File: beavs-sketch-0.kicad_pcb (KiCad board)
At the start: 2 copper layers, 25 parts, among them J1 USB_C_Receptacle_USB2.0_16P, J10 Conn_01x03, J11 Conn_01x03, J2 Conn_Coaxial, J3 Micro_SD_Card_Det2, J4 Conn_Coaxial, J5 Conn_01x02, J6 Conn_01x03, J7 Conn_01x03, J8 Conn_01x03, J9 Conn_01x03, U1 RP2040, U2 W25Q128JVS, U3 MS5607-02BA, U4 RFM95W-915S2, U5 MAX-M10S, Y1 Crystal_GND24

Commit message: do some schematic work
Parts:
- removed REF**: JST_VH_B3P-VH-B_1x03_P3.96mm_Vertical, Connector_JST:JST_VH_B3P-VH-B_1x03_P3.96mm_Vertical
- added C10: 100n, Capacitor_SMD:C_0402_1005Metric, F.Cu at (204.8, 132.0)
- added C11: 1u, Capacitor_SMD:C_0402_1005Metric, F.Cu at (211.0, 130.1)
- added C12: 100n, Capacitor_SMD:C_0402_1005Metric, F.Cu at (200.7, 128.0)
- added C13: 100n, Capacitor_SMD:C_0402_1005Metric, F.Cu at (210.9, 126.3)
- added C14: 100n, Capacitor_SMD:C_0402_1005Metric, F.Cu at (200.3, 126.8)
- added C4: 100n, Capacitor_SMD:C_0402_1005Metric, F.Cu at (210.2, 154.4)
- added C5: 100n, Capacitor_SMD:C_0402_1005Metric, F.Cu at (207.9, 154.9)
- added C6: 1u, Capacitor_SMD:C_0402_1005Metric, F.Cu at (210.0, 130.1)
- added C7: 100n, Capacitor_SMD:C_0402_1005Metric, F.Cu at (209.1, 131.1)
- added C8: 100n, Capacitor_SMD:C_0402_1005Metric, F.Cu at (204.7, 120.3)
- added C9: 100n, Capacitor_SMD:C_0402_1005Metric, F.Cu at (208.7, 120.7)
- added J12: Micro_SD_Card, Connector_Card:microSD_HC_Molex_47219-2001, F.Cu at (205.1, 141.7)
- added NT1: NetTie_2, NetTie:NetTie-2_SMD_Pad2.0mm, F.Cu at (183.8, 56.6)
- added Q2: SiS427EDN, Package_SO:Vishay_PowerPAK_1212-8_Single, F.Cu at (188.0, 46.5)
- added R2: R_Small, Resistor_SMD:R_0402_1005Metric, F.Cu at (191.2, 45.3)
- added R3: 5.1k, Resistor_SMD:R_0402_1005Metric, F.Cu at (214.0, 142.0)
- added R4: DNF, Resistor_SMD:R_0402_1005Metric, F.Cu at (207.5, 131.4)
- added R5: 5.1k, Resistor_SMD:R_0402_1005Metric, F.Cu at (214.0, 130.2)
- added U10: INA745A, beavs-footprints:QFN-14-REL_TI, F.Cu at (193.4, 82.6)
- added U11: INA745A, beavs-footprints:QFN-14-REL_TI, F.Cu at (193.4, 93.2)
- added U12: INA745A, beavs-footprints:QFN-14-REL_TI, F.Cu at (193.4, 103.7)
- added U13: INA745A, beavs-footprints:QFN-14-REL_TI, F.Cu at (193.4, 114.2)
- added U14: ISM6HG256X, Package_LGA:LGA-14_3x2.5mm_P0.5mm_LayoutBorder3x4y, F.Cu at (207.9, 152.9)
- added U15: SN74LVC8T245, Package_SO:TSSOP-24_4.4x7.8mm_P0.65mm, F.Cu at (191.4, 133.3)
- added U6: INA745A, beavs-footprints:QFN-14-REL_TI, F.Cu at (193.4, 61.1)
- added U7: AMS1117-3.3, Package_TO_SOT_SMD:SOT-223-3_TabPin2, F.Cu at (221.7, 113.0)
- added U8: AMS1117-5.0, Package_TO_SOT_SMD:SOT-223-3_TabPin2, F.Cu at (214.0, 113.0)
- added U9: INA745A, beavs-footprints:QFN-14-REL_TI, F.Cu at (193.4, 71.6)
- J10, J11, J6, J7, J8, J9: footprint Connector_JST:JST_XH_B3B-XH-AM_1x03_P2.50mm_Vertical -> Connector_JST:JST_VH_B3P-VH-B_1x03_P3.96mm_Vertical
- J3: value Micro_SD_Card_Det2 -> Conn_01x02; footprint Connector_Card:microSD_HC_Hirose_DM3AT-SF-PEJM5 -> Connector_AMASS:AMASS_XT30UPB-F_1x02_P5.0mm_Vertical
- J5: footprint Connector_JST:JST_XH_S2B-XH-A-1_1x02_P2.50mm_Horizontal -> Connector_JST:JST_XH_B2B-XH-A_1x02_P2.50mm_Vertical
- moved D1 90.5 mm to (180.2, 160.8), turned to -90 degrees
- moved D2 87.8 mm to (180.2, 157.3), turned to -90 degrees
- moved D3 85.3 mm to (180.2, 153.7), turned to -90 degrees
- moved D4 83.0 mm to (180.2, 150.2), turned to -90 degrees
- moved D5 81.0 mm to (180.2, 146.6), turned to -90 degrees
- moved D6 79.3 mm to (180.2, 143.1), turned to -90 degrees
- moved J5 68.3 mm to (182.3, 129.2), turned to 90 degrees
- moved R1 66.7 mm to (200.6, 125.8)
- moved J1 53.9 mm to (218.4, 136.0), turned to 90 degrees
- moved U3 52.4 mm to (201.7, 153.8), turned to 180 degrees
- moved J4 51.7 mm to (224.0, 81.1), turned to 0 degrees
- moved J2 51.2 mm to (202.1, 159.5)
- moved U5 51.1 mm to (192.8, 156.2)
- moved J3 46.0 mm to (182.5, 46.5), turned to -90 degrees
- moved U2 43.2 mm to (219.3, 123.8), turned to -90 degrees
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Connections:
- net /SCL renamed /Sensors/SCL
- net /SDA renamed /Sensors/SDA
- net /~{RESET} renamed /mcu/~{RESET}
- net Net-(U3-CSB-Pad4) renamed /Sensors/BARO_CS
- J1 pad A1: Net-(J1-GND-PadA1) -> GND
- J1 pad A12: Net-(J1-GND-PadA1) -> GND
- J1 pad A5: unconnected-(J1-CC1-PadA5) -> Net-(J1-CC1)
- J1 pad A6: unconnected-(J1-D+-PadA6) -> /mcu/USB_D+
- J1 pad A7: unconnected-(J1-D--PadA7) -> /mcu/USB_D-
- J1 pad B1: Net-(J1-GND-PadA1) -> GND
- J1 pad B12: Net-(J1-GND-PadA1) -> GND
- J1 pad B5: unconnected-(J1-CC2-PadB5) -> Net-(J1-CC2)
- J1 pad B6: unconnected-(J1-D+-PadB6) -> /mcu/USB_D+
- J1 pad B7: unconnected-(J1-D--PadB7) -> /mcu/USB_D-
- J1 pad S1: unconnected-(J1-SHIELD-PadS1) -> GND
- J10 pad 2: unconnected-(J10-Pin_2-Pad2) -> GND1
- J10 pad 3: unconnected-(J10-Pin_3-Pad3) -> Net-(J10-Pin_3)
- J11 pad 2: unconnected-(J11-Pin_2-Pad2) -> GND1
- J11 pad 3: unconnected-(J11-Pin_3-Pad3) -> Net-(J11-Pin_3)
- J3 pad 1: unconnected-(J3-DAT2-Pad1) -> Net-(J3-Pin_1)
- J3 pad 2: unconnected-(J3-DAT3/CD-Pad2) -> GND
- J6 pad 2: unconnected-(J6-Pin_2-Pad2) -> GND1
- J6 pad 3: unconnected-(J6-Pin_3-Pad3) -> Net-(J6-Pin_3)
- J7 pad 2: unconnected-(J7-Pin_2-Pad2) -> GND1
- J7 pad 3: unconnected-(J7-Pin_3-Pad3) -> Net-(J7-Pin_3)
- J8 pad 2: unconnected-(J8-Pin_2-Pad2) -> GND1
- J8 pad 3: unconnected-(J8-Pin_3-Pad3) -> Net-(J8-Pin_3)
- J9 pad 2: unconnected-(J9-Pin_2-Pad2) -> GND1
- J9 pad 3: unconnected-(J9-Pin_3-Pad3) -> Net-(J9-Pin_3)
- U1 pad 1: Net-(U1-IOVDD-Pad1) -> +3V3
- U1 pad 10: Net-(U1-IOVDD-Pad1) -> +3V3
- U1 pad 22: Net-(U1-IOVDD-Pad1) -> +3V3
- U1 pad 23: Net-(U1-DVDD-Pad23) -> +1V1
- U1 pad 29: unconnected-(U1-GPIO18-Pad29) -> /SD Card/CMD
- U1 pad 30: unconnected-(U1-GPIO19-Pad30) -> /SD Card/DAT0
- U1 pad 31: unconnected-(U1-GPIO20-Pad31) -> /SD Card/DAT1
- U1 pad 32: unconnected-(U1-GPIO21-Pad32) -> /SD Card/DAT2
- U1 pad 33: Net-(U1-IOVDD-Pad1) -> +3V3
- U1 pad 34: unconnected-(U1-GPIO22-Pad34) -> /SD Card/DAT3
- U1 pad 35: unconnected-(U1-GPIO23-Pad35) -> /SD Card/CLK
- U1 pad 42: Net-(U1-IOVDD-Pad1) -> +3V3
- U1 pad 43: unconnected-(U1-ADC_AVDD-Pad43) -> +3V3
- U1 pad 44: unconnected-(U1-VREG_IN-Pad44) -> +3V3
- U1 pad 45: unconnected-(U1-VREG_VOUT-Pad45) -> +1V1
- U1 pad 46: /USB_D- -> /mcu/USB_D-
- U1 pad 47: /USB_D+ -> /mcu/USB_D+
- U1 pad 48: unconnected-(U1-USB_VDD-Pad48) -> +3V3
- U1 pad 49: Net-(U1-IOVDD-Pad1) -> +3V3
- U1 pad 50: Net-(U1-DVDD-Pad23) -> +1V1
- U2 pad 4: unconnected-(U2-GND-Pad4) -> GND
- U3 pad 2: unconnected-(U3-PS-Pad2) -> GND
- U3 pad 6: unconnected-(U3-SDO-Pad6) -> /Sensors/MISO
- U3 pad 7: unconnected-(U3-SDI/SDA-Pad7) -> /Sensors/MOSI
- U3 pad 8: unconnected-(U3-SCLK-Pad8) -> /Sensors/SCK
- Y1 pad 2: unconnected-(Y1-Pad2) -> GND
- Y1 pad 4: unconnected-(Y1-Pad4) -> GND
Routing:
- net /servos/SCL: track 0.00 -> 64.2 mm, vias 0 -> 6
- net /servos/SDA: track 0.00 -> 58.3 mm, vias 0 -> 6
- net +3V3: track 0.00 -> 31.5 mm, vias 0 -> 21
- net +1V1: track 0.00 -> 19.7 mm, vias 0 -> 3
- net Net-(U1-QSPI_SS): track 0.00 -> 16.0 mm
- net Net-(U1-QSPI_SD2): track 0.00 -> 16.0 mm
- net Net-(U1-QSPI_SD1): track 0.00 -> 15.9 mm
- net Net-(U1-QSPI_SD3): track 0.00 -> 15.9 mm
- net Net-(U1-QSPI_SCLK): track 0.00 -> 15.9 mm
- net Net-(U1-QSPI_SD0): track 0.00 -> 15.9 mm
- net /mcu/USB_D+: track 0.00 -> 14.6 mm
- net /mcu/USB_D-: track 0.00 -> 14.4 mm
- net /SD Card/DAT1: track 0.00 -> 14.0 mm, vias 0 -> 2
- net /SD Card/DAT0: track 0.00 -> 12.3 mm, vias 0 -> 2
- net /Sensors/SCK: track 0.00 -> 12.3 mm, vias 0 -> 2
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- added copper zone on In2.Cu, net +3V3
- added copper zone on B.Cu, net +BATT
- added copper zone on F.Cu, net +BATT
- added copper zone on B.Cu, net GND
- added copper zone on F.Cu, net GND
- added copper zone on In1.Cu, net GND
- added copper zone on B.Cu, net GND1
- added copper zone on F.Cu, net GND1
- added copper zone on B.Cu, net Net-(J3-Pin_1)
- added copper zone on F.Cu, net Net-(J3-Pin_1)
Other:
- board outline added: 51.9 x 165.1 mm
- copper layers 2 -> 4

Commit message: got it to fit in about the right shape
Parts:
- added REF**: MountingHole_2.2mm_M2, MountingHole:MountingHole_2.2mm_M2, F.Cu at (214.0, 56.4)
- added REF**: MountingHole_2.2mm_M2, MountingHole:MountingHole_2.2mm_M2, F.Cu at (186.8, 120.8)
- added REF**: MountingHole_2.2mm_M2, MountingHole:MountingHole_2.2mm_M2, F.Cu at (184.8, 55.5)
- added REF**: MountingHole_2.2mm_M2, MountingHole:MountingHole_2.2mm_M2, F.Cu at (218.5, 117.7)
- moved D3 85.1 mm to (203.6, 71.8)
- moved D1 85.1 mm to (203.6, 78.9)
- moved D4 85.1 mm to (203.6, 68.3)
- moved D6 85.1 mm to (203.6, 61.2)
- moved D2 85.1 mm to (203.6, 75.4)
- moved D5 85.1 mm to (203.6, 64.7)
- moved J1 53.7 mm to (222.9, 82.5)
- moved R3 53.7 mm to (218.5, 88.5)
- moved R5 53.7 mm to (218.5, 76.7)
- moved U15 50.8 mm to (222.3, 93.0), turned to 90 degrees
- moved U2 45.3 mm to (210.4, 79.4), turned to 0 degrees
- moved C11 44.9 mm to (214.6, 85.4), turned to 0 degrees
- moved C7 44.3 mm to (215.6, 87.3), turned to 0 degrees
- moved C6 44.0 mm to (214.6, 86.3), turned to 0 degrees
- moved R4 42.4 mm to (215.4, 89.7), turned to 90 degrees
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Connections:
- U15 pad 1: unconnected-(U15-V_{CCA}-Pad1) -> +3V3
- U15 pad 11: Net-(U15-GND-Pad11) -> GND
- U15 pad 12: Net-(U15-GND-Pad11) -> GND
- U15 pad 13: Net-(U15-GND-Pad11) -> GND
- U15 pad 23: Net-(U15-V_{CCB}-Pad23) -> +5V
- U15 pad 24: Net-(U15-V_{CCB}-Pad23) -> +5V
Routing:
- net +5V: track 0.00 -> 42.2 mm, vias 0 -> 7
- net /servos/SCL: track 64.2 -> 57.0 mm
- net /servos/SDA: track 58.3 -> 51.5 mm
- net Net-(U1-QSPI_SD0): track 15.9 -> 9.13 mm
- net Net-(U1-QSPI_SD2): track 16.0 -> 9.24 mm
- net /SD Card/CLK: track 11.2 -> 17.6 mm, vias 0 -> 2
- net Net-(U1-QSPI_SD1): track 15.9 -> 10.3 mm
- net +1V1: track 19.7 -> 15.3 mm, vias 3 -> 0
- net Net-(U1-QSPI_SCLK): track 15.9 -> 11.5 mm
- net Net-(U1-QSPI_SS): track 16.0 -> 11.7 mm
- net /SD Card/DAT2: track 11.2 -> 14.7 mm, vias 0 -> 2
- net Net-(U1-QSPI_SD3): track 15.9 -> 12.7 mm
- net /Sensors/MISO: track 9.29 -> 6.66 mm
- net /SD Card/DAT3: track 11.2 -> 13.5 mm, vias 0 -> 2
- net +3V3: track 31.5 -> 29.3 mm
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- removed copper zone on B.Cu, net +BATT
- removed copper zone on B.Cu, net GND1
- removed copper zone on F.Cu, net GND1
- removed copper zone on B.Cu, net Net-(J3-Pin_1)
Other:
- board size 51.9 x 165.1 mm -> 76 x 76 mm

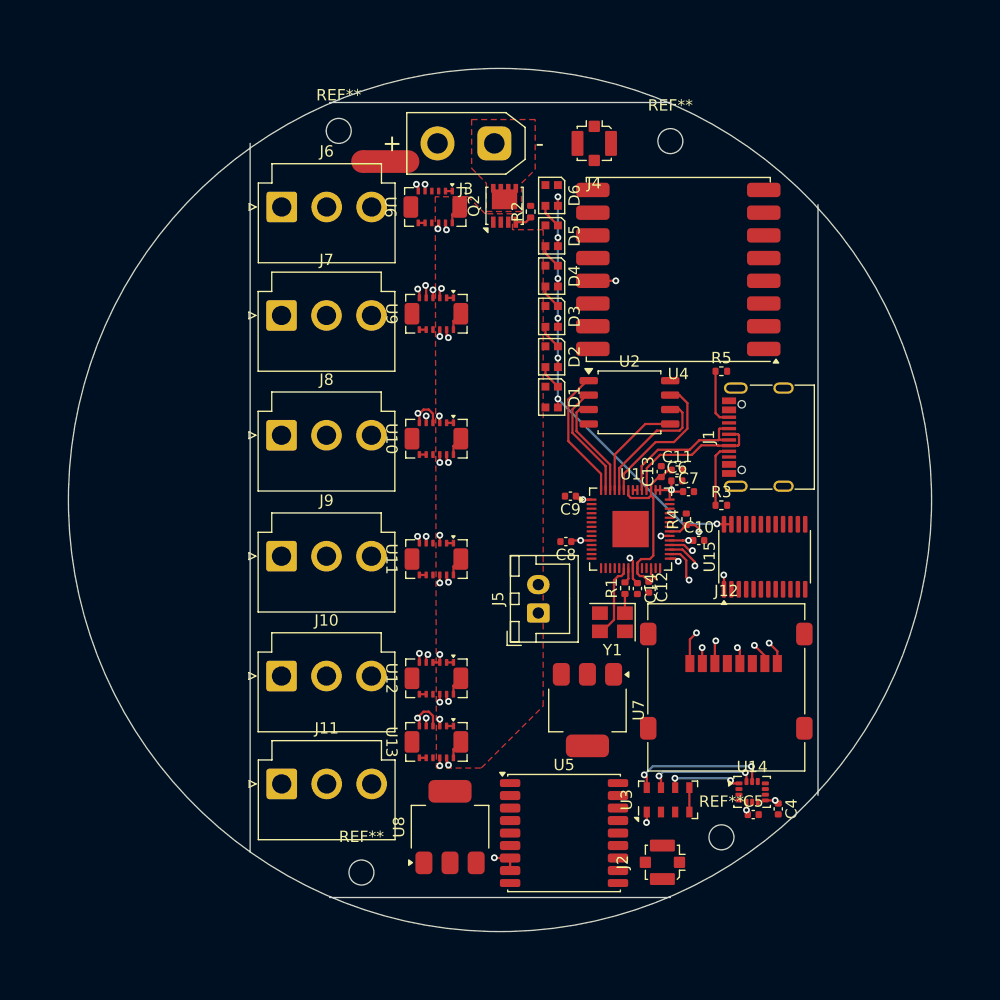
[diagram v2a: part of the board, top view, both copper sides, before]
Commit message: importing CAD edge cuts
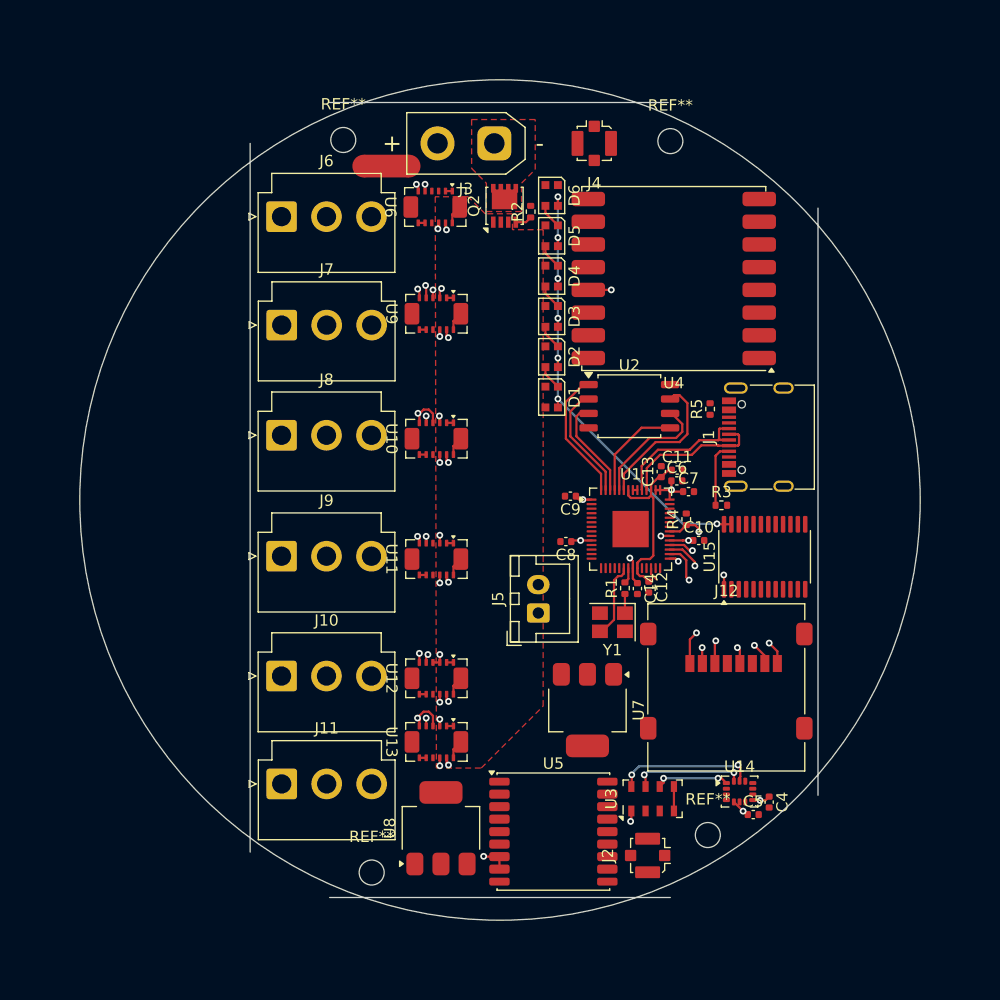
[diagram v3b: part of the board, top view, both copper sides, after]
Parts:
- moved R5 3.47 mm to (217.5, 80.0), turned to 90 degrees
- moved J2 1.43 mm to (212.0, 119.3)
- moved U3 1.36 mm to (212.4, 114.3)
- moved REF** 1.22 mm to (217.3, 117.5)
- moved U14 1.11 mm to (220.1, 113.7)
- moved C4 1.00 mm to (222.7, 114.6)
- moved U5 0.95 mm to (203.7, 117.2)
- moved REF** 0.90 mm to (187.7, 120.8)
- moved REF** 0.89 mm to (185.2, 56.3)
- moved U4 0.89 mm to (214.3, 68.5)
- moved J6 0.85 mm to (179.8, 63.0)
- moved J7 0.85 mm to (179.8, 72.6)
- moved U8 0.81 mm to (193.8, 116.9)
- moved NT1 0.41 mm to (189.0, 58.6)
- moved U2 0.34 mm to (210.4, 79.7)
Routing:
- net Net-(J1-CC2): track 5.02 -> 0.00 mm
- net +3V3: track 29.3 -> 30.2 mm
- net Net-(U1-QSPI_SCLK): track 11.5 -> 10.9 mm
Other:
- board size 76 x 76 mm -> 74 x 74 mm

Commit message: add 3d models and do other stuff
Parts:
- added C1: C_Small, Capacitor_SMD:C_0402_1005Metric, F.Cu at (212.7, 96.6)
- added C15: 10u, Capacitor_SMD:C_0603_1608Metric, F.Cu at (195.7, 122.1)
- added C16: 22u, Capacitor_SMD:C_0603_1608Metric, F.Cu at (192.3, 122.1)
- added C17: 22u, Capacitor_SMD:C_0603_1608Metric, F.Cu at (206.6, 111.6)
- added C18: 10u, Capacitor_SMD:C_0603_1608Metric, F.Cu at (207.8, 101.3)
- added C19: 100n, Capacitor_SMD:C_0402_1005Metric, F.Cu at (193.8, 64.9)
- added C2: C_Small, Capacitor_SMD:C_0402_1005Metric, F.Cu at (210.2, 101.0)
- added C20: 100n, Capacitor_SMD:C_0402_1005Metric, F.Cu at (194.0, 74.3)
- added C21: 100n, Capacitor_SMD:C_0402_1005Metric, F.Cu at (194.1, 85.3)
- added C22: 100n, Capacitor_SMD:C_0402_1005Metric, F.Cu at (194.1, 112.0)
- added C23: 100n, Capacitor_SMD:C_0402_1005Metric, F.Cu at (194.1, 106.5)
- added C24: 100n, Capacitor_SMD:C_0402_1005Metric, F.Cu at (194.1, 95.9)
- added D7: D_Schottky, Diode_SMD:D_SOD-123, F.Cu at (202.4, 105.2)
- added D8: D_Schottky, Diode_SMD:D_SOD-123, F.Cu at (202.4, 110.0)
- added R6: R_Small, Resistor_SMD:R_0402_1005Metric, F.Cu at (201.7, 101.4)
- added R7: R_Small, Resistor_SMD:R_0402_1005Metric, F.Cu at (203.6, 101.4)
- J10, J11, J6, J7, J8, J9: footprint Connector_JST:JST_VH_B3P-VH-B_1x03_P3.96mm_Vertical -> beavs-footprints:JST_VH_B3P-VH-B_1x03_P3.96mm_Vertical_model
- moved REF** 1.28 mm to (213.2, 57.4)
- moved R4 0.91 mm to (216.3, 89.8)
- moved U7 0.70 mm to (207.4, 106.5)
- moved C12 0.62 mm to (212.7, 95.7), turned to 0 degrees
- moved J4 0.51 mm to (206.8, 56.5)
- moved U5 0.50 mm to (203.7, 117.7)
- moved C14 0.14 mm to (211.0, 95.7)
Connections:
- net Net-(J1-VBUS-PadA4) renamed VBUS
- D1 pad 3: unconnected-(D1-DIN-Pad3) -> Net-(D1-DIN)
- J10 pad 1: unconnected-(J10-Pin_1-Pad1) -> /servos/S5
- J11 pad 1: unconnected-(J11-Pin_1-Pad1) -> /servos/S6
- J5 pad 1: /ARM_SWITCH -> GND
- J5 pad 2: GND -> /ARM_SWITCH
- J6 pad 1: unconnected-(J6-Pin_1-Pad1) -> /servos/S1
- J7 pad 1: unconnected-(J7-Pin_1-Pad1) -> /servos/S2
- J8 pad 1: unconnected-(J8-Pin_1-Pad1) -> /servos/S3
- J9 pad 1: unconnected-(J9-Pin_1-Pad1) -> /servos/S4
- U1 pad 12: unconnected-(U1-GPIO9-Pad12) -> /Radio/MOSI
- U1 pad 13: unconnected-(U1-GPIO10-Pad13) -> /Radio/MISO
- U1 pad 14: unconnected-(U1-GPIO11-Pad14) -> /Radio/SCK
- U1 pad 15: unconnected-(U1-GPIO12-Pad15) -> /mcu/M_LED_D
- U1 pad 16: unconnected-(U1-GPIO13-Pad16) -> /Sensors/BARO_CS
- U1 pad 17: unconnected-(U1-GPIO14-Pad17) -> /Sensors/IMU_CS
- U1 pad 2: unconnected-(U1-GPIO0-Pad2) -> /Radio/CS
- U1 pad 27: unconnected-(U1-GPIO16-Pad27) -> /mcu/M_S6
- U1 pad 28: unconnected-(U1-GPIO17-Pad28) -> /mcu/M_S5
- U1 pad 3: unconnected-(U1-GPIO1-Pad3) -> /Radio/D0
- U1 pad 36: unconnected-(U1-GPIO24-Pad36) -> /mcu/M_S4
- U1 pad 37: unconnected-(U1-GPIO25-Pad37) -> /mcu/M_S3
- U1 pad 38: unconnected-(U1-GPIO26_ADC0-Pad38) -> /mcu/BATTERY_SENSE
- U1 pad 4: unconnected-(U1-GPIO2-Pad4) -> /Radio/RESET
- U1 pad 40: unconnected-(U1-GPIO28_ADC2-Pad40) -> /mcu/M_S1
- U1 pad 41: unconnected-(U1-GPIO29_ADC3-Pad41) -> /mcu/M_S2
- U1 pad 6: unconnected-(U1-GPIO4-Pad6) -> /Sensors/SDA
- U1 pad 7: unconnected-(U1-GPIO5-Pad7) -> /Sensors/SCL
- U1 pad 8: unconnected-(U1-GPIO6-Pad8) -> /ARM_SWITCH
- U10 pad 4: /servos/SCL -> /Sensors/SCL
- U10 pad 5: /servos/SDA -> /Sensors/SDA
- U10 pad 6: /servos/SCL -> /Sensors/SCL
- U11 pad 5: /servos/SDA -> /Sensors/SDA
- U11 pad 6: /servos/SCL -> /Sensors/SCL
- U12 pad 5: /servos/SDA -> /Sensors/SDA
- U12 pad 6: /servos/SCL -> /Sensors/SCL
- U13 pad 4: /servos/SCL -> /Sensors/SCL
- U13 pad 5: /servos/SDA -> /Sensors/SDA
- U13 pad 6: /servos/SCL -> /Sensors/SCL
- U14 pad 1: /Sensors/MISO -> /Radio/MISO
- U14 pad 13: /Sensors/SCK -> /Radio/SCK
- U14 pad 14: /Sensors/MOSI -> /Radio/MOSI
- U15 pad 15: unconnected-(U15-B7-Pad15) -> Net-(D1-DIN)
- U15 pad 16: unconnected-(U15-B6-Pad16) -> /servos/S6
- U15 pad 17: unconnected-(U15-B5-Pad17) -> /servos/S5
- U15 pad 18: unconnected-(U15-B4-Pad18) -> /servos/S4
- U15 pad 19: unconnected-(U15-B3-Pad19) -> /servos/S3
- U15 pad 20: unconnected-(U15-B2-Pad20) -> /servos/S2
- U15 pad 21: unconnected-(U15-B1-Pad21) -> /servos/S1
- U15 pad 3: unconnected-(U15-A1-Pad3) -> /mcu/M_S1
- U15 pad 4: unconnected-(U15-A2-Pad4) -> /mcu/M_S2
- U15 pad 5: unconnected-(U15-A3-Pad5) -> /mcu/M_S3
- U15 pad 6: unconnected-(U15-A4-Pad6) -> /mcu/M_S4
- U15 pad 7: unconnected-(U15-A5-Pad7) -> /mcu/M_S5
- U15 pad 8: unconnected-(U15-A6-Pad8) -> /mcu/M_S6
- U15 pad 9: unconnected-(U15-A7-Pad9) -> /mcu/M_LED_D
- U3 pad 6: /Sensors/MISO -> /Radio/MISO
- U3 pad 7: /Sensors/MOSI -> /Radio/MOSI
- U3 pad 8: /Sensors/SCK -> /Radio/SCK
- U4 pad 14: unconnected-(U4-DIO0-Pad14) -> /Radio/D0
- U4 pad 2: unconnected-(U4-MISO-Pad2) -> /Radio/MISO
- U4 pad 3: unconnected-(U4-MOSI-Pad3) -> /Radio/MOSI
- U4 pad 4: unconnected-(U4-SCK-Pad4) -> /Radio/SCK
- U4 pad 5: unconnected-(U4-NSS-Pad5) -> /Radio/CS
- U4 pad 6: unconnected-(U4-RESET-Pad6) -> /Radio/RESET
- U6 pad 5: /servos/SDA -> /Sensors/SDA
- U6 pad 6: /servos/SCL -> /Sensors/SCL
- U7 pad 1: unconnected-(U7-GND-Pad1) -> GND
- U7 pad 2: unconnected-(U7-VO-Pad2) -> +3V3
- U7 pad 3: unconnected-(U7-VI-Pad3) -> Net-(D7-K)
- U8 pad 1: unconnected-(U8-GND-Pad1) -> GND
- U8 pad 2: unconnected-(U8-VO-Pad2) -> +5V
- U8 pad 3: unconnected-(U8-VI-Pad3) -> Net-(D7-K)
- U9 pad 5: /servos/SDA -> /Sensors/SDA
- U9 pad 6: /servos/SCL -> /Sensors/SCL
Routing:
- net /Sensors/SCL: track 0.00 -> 95.2 mm, vias 0 -> 9
- net /Sensors/SDA: track 0.00 -> 91.8 mm, vias 0 -> 9
- net /Radio/SCK: track 0.00 -> 86.3 mm, vias 0 -> 5
- net /servos/S6: track 0.00 -> 86.3 mm, vias 0 -> 3
- net /Radio/MOSI: track 0.00 -> 83.8 mm, vias 0 -> 5
- net /Radio/MISO: track 0.00 -> 80.0 mm, vias 0 -> 5
- net /servos/S5: track 0.00 -> 75.4 mm, vias 0 -> 3
- net /servos/S1: track 0.00 -> 66.0 mm, vias 0 -> 3
- net VBUS: track 0.00 -> 59.8 mm, vias 0 -> 3
- net /servos/S4: track 0.00 -> 59.1 mm, vias 0 -> 3
- net /servos/SCL: track 57.0 -> 0.00 mm, vias 6 -> 0
- net /servos/S2: track 0.00 -> 54.9 mm, vias 0 -> 3
- net /servos/SDA: track 51.5 -> 0.00 mm, vias 6 -> 0
- net /servos/S3: track 0.00 -> 49.2 mm, vias 0 -> 2
- net /Radio/RESET: track 0.00 -> 46.3 mm, vias 0 -> 2
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- added copper zone on F.Cu, net +3V3
- added copper zone on B.Cu, net GND1
- added copper zone on F.Cu, net GND1
- added copper zone on F.Cu, net Net-(J10-Pin_3)
- added copper zone on F.Cu, net Net-(J11-Pin_3)
- added copper zone on F.Cu, net Net-(J6-Pin_3)
- added copper zone on F.Cu, net Net-(J7-Pin_3)
- added copper zone on F.Cu, net Net-(J8-Pin_3)
- added copper zone on F.Cu, net Net-(J9-Pin_3)
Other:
- board size 74 x 74 mm -> 50 x 70 mm

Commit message: add some TVS diodes
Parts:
- added NT2: NetTie_2, NetTie:NetTie-2_SMD_Pad2.0mm, B.Cu at (183.8, 61.5)
- added NT3: NetTie_2, NetTie:NetTie-2_SMD_Pad2.0mm, F.Cu at (183.8, 61.8)
- added NT4: NetTie_2, NetTie:NetTie-2_SMD_Pad2.0mm, F.Cu at (182.5, 61.8)
- added NT5: NetTie_2, NetTie:NetTie-2_SMD_Pad2.0mm, B.Cu at (185.0, 61.5)
- added NT6: NetTie_2, NetTie:NetTie-2_SMD_Pad2.0mm, B.Cu at (182.5, 61.5)
- added R8: 5.1k, Resistor_SMD:R_0402_1005Metric, F.Cu at (203.8, 89.5)
- added R9: 5.1k, Resistor_SMD:R_0402_1005Metric, F.Cu at (203.8, 90.5)
- added U16: SRV05-4, Package_TO_SOT_SMD:SOT-23-6, F.Cu at (203.8, 85.2)
- moved NT1 5.09 mm to (185.0, 61.8), turned to 90 degrees
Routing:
- net /servos/S3: track 49.2 -> 58.8 mm
- net /servos/S4: track 59.1 -> 64.8 mm, vias 3 -> 4
- net /servos/S2: track 54.9 -> 60.3 mm
- net +5V: track 86.0 -> 89.9 mm
- net /servos/S1: track 66.0 -> 68.0 mm
- net +3V3: track 38.7 -> 40.6 mm, vias 28 -> 29
- net GND: track 11.0 -> 12.2 mm, vias 67 -> 68
- net /Sensors/SDA: track 91.8 -> 92.5 mm
- net /Sensors/SCL: track 95.2 -> 95.8 mm
- net Net-(U1-QSPI_SD3): track 13.2 -> 12.6 mm
